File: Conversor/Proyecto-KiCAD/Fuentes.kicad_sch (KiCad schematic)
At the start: 17 parts, among them J6 Barrel_Jack_Switch, P1 SW_SPDT, P2 5V Header, P3 5V Header, P4 Jumper 2, U1 LP2985-3.3, U11 LM7805_TO252, U13 THB3-1211

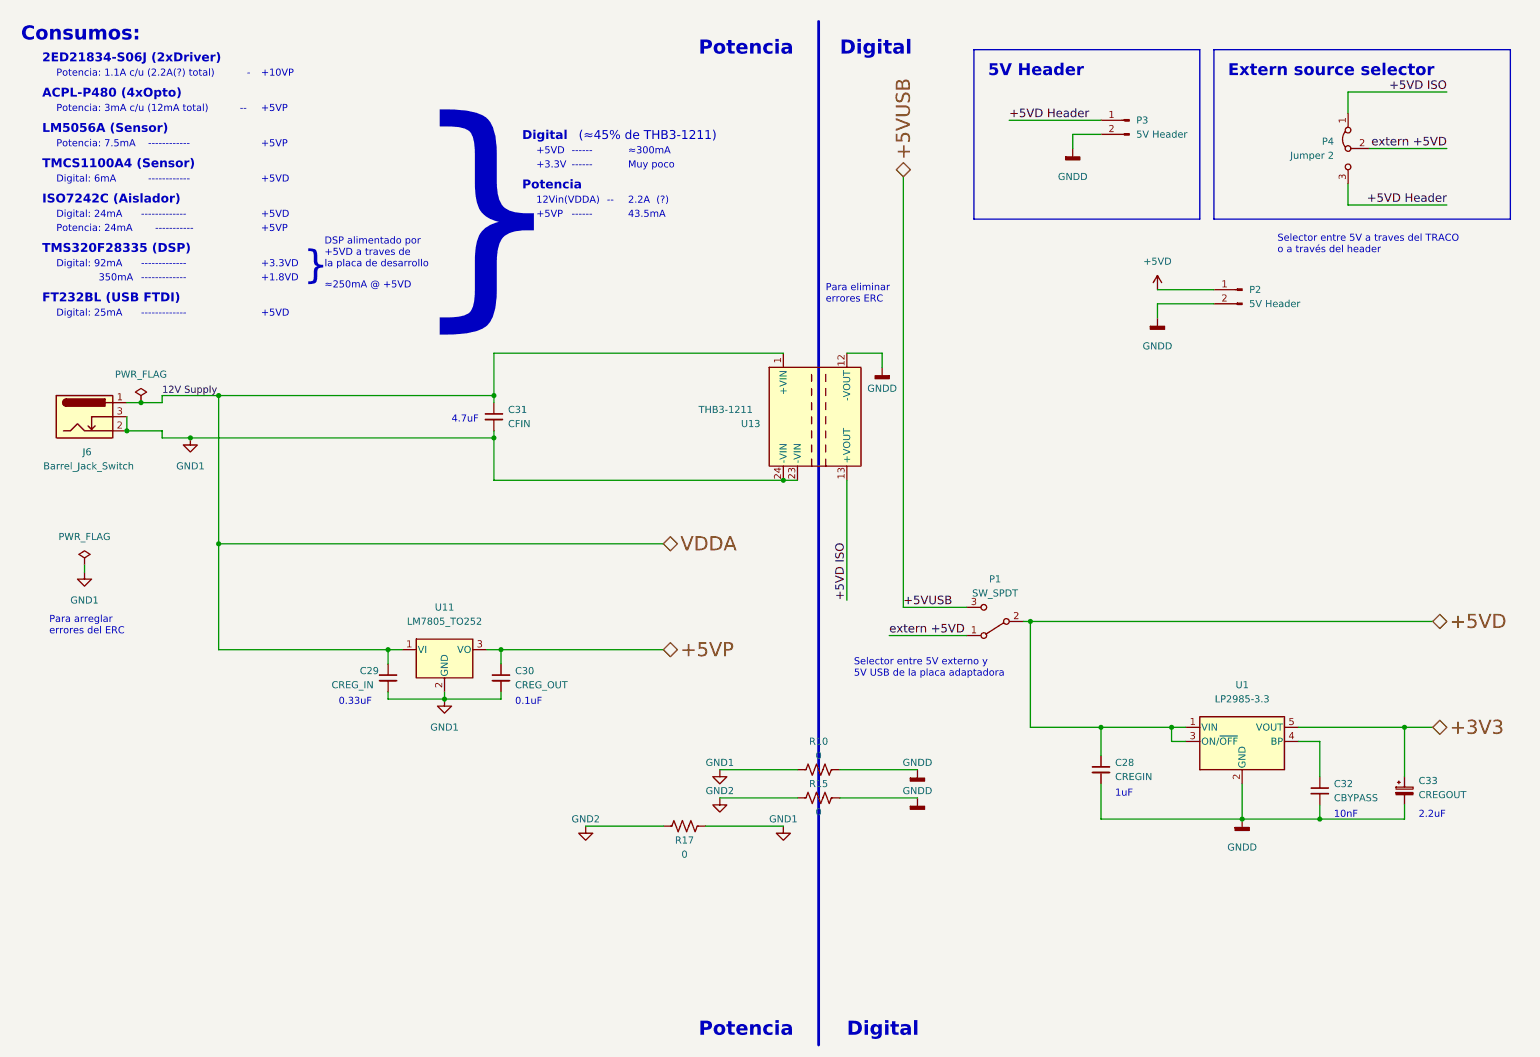
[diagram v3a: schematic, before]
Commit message: Agregar el selector de alim. de 12V y seguir emprolijando la placa
- Agregar modelos de los switches
- Agregar algunos test points
Por hacer:
  - Todo lo de los dos anteriores commits
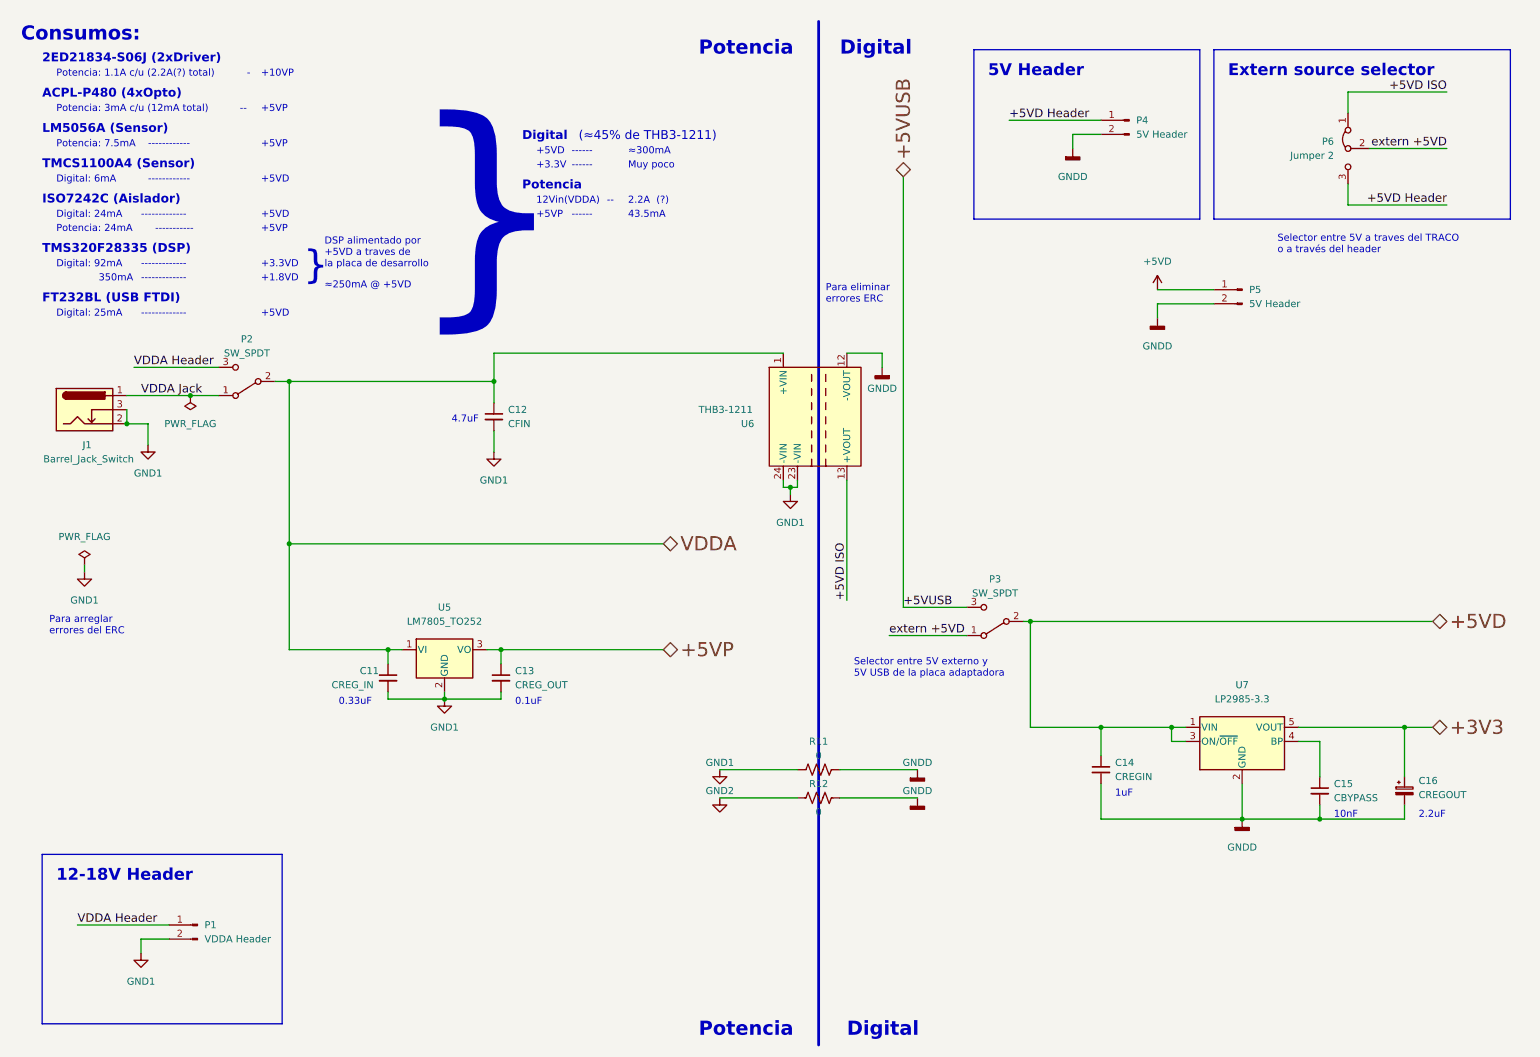
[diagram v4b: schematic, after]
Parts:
- removed R17: 0, Resistor_SMD:R_1206_3216Metric_Pad1.30x1.75mm_HandSolder, symbol Device:R_US
- added P1: VDDA Header, Connector_PinHeader_2.54mm:PinHeader_1x02_P2.54mm_Vertical, symbol Connector:Conn_01x02_Male
- added P2: SW_SPDT, Connector_PinHeader_2.54mm:PinHeader_1x03_P2.54mm_Vertical, symbol Switch:SW_SPDT
- renumbered C29 to C11, C31 to C12, C30 to C13, C28 to C14, C32 to C15, C33 to C16, J6 to J1, P1 to P3, P3 to P4, P2 to P5, P4 to P6, R10 to R11, R15 to R12, U11 to U5, U13 to U6, U1 to U7
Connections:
- net GND1: now also P1.2 (Pin_2)
- net VDDA: now also P2.2 (B); no longer J1.1
- new net VDDA Header: P1.1 (Pin_1), P2.3 (C)
- new net VDDA Jack: J1.1, P2.1 (A)
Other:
- note added: "12-18V Header"
- moved on the sheet: J1

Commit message: Agregar conectores de 12V y 5V, y seguir mas layout recommendations
- Ademas, seguir emprolijando la placa
- Agregar esquinas redondeadas a la placa
- Por hacer:
  - Ver las recomendaciones de Jorge
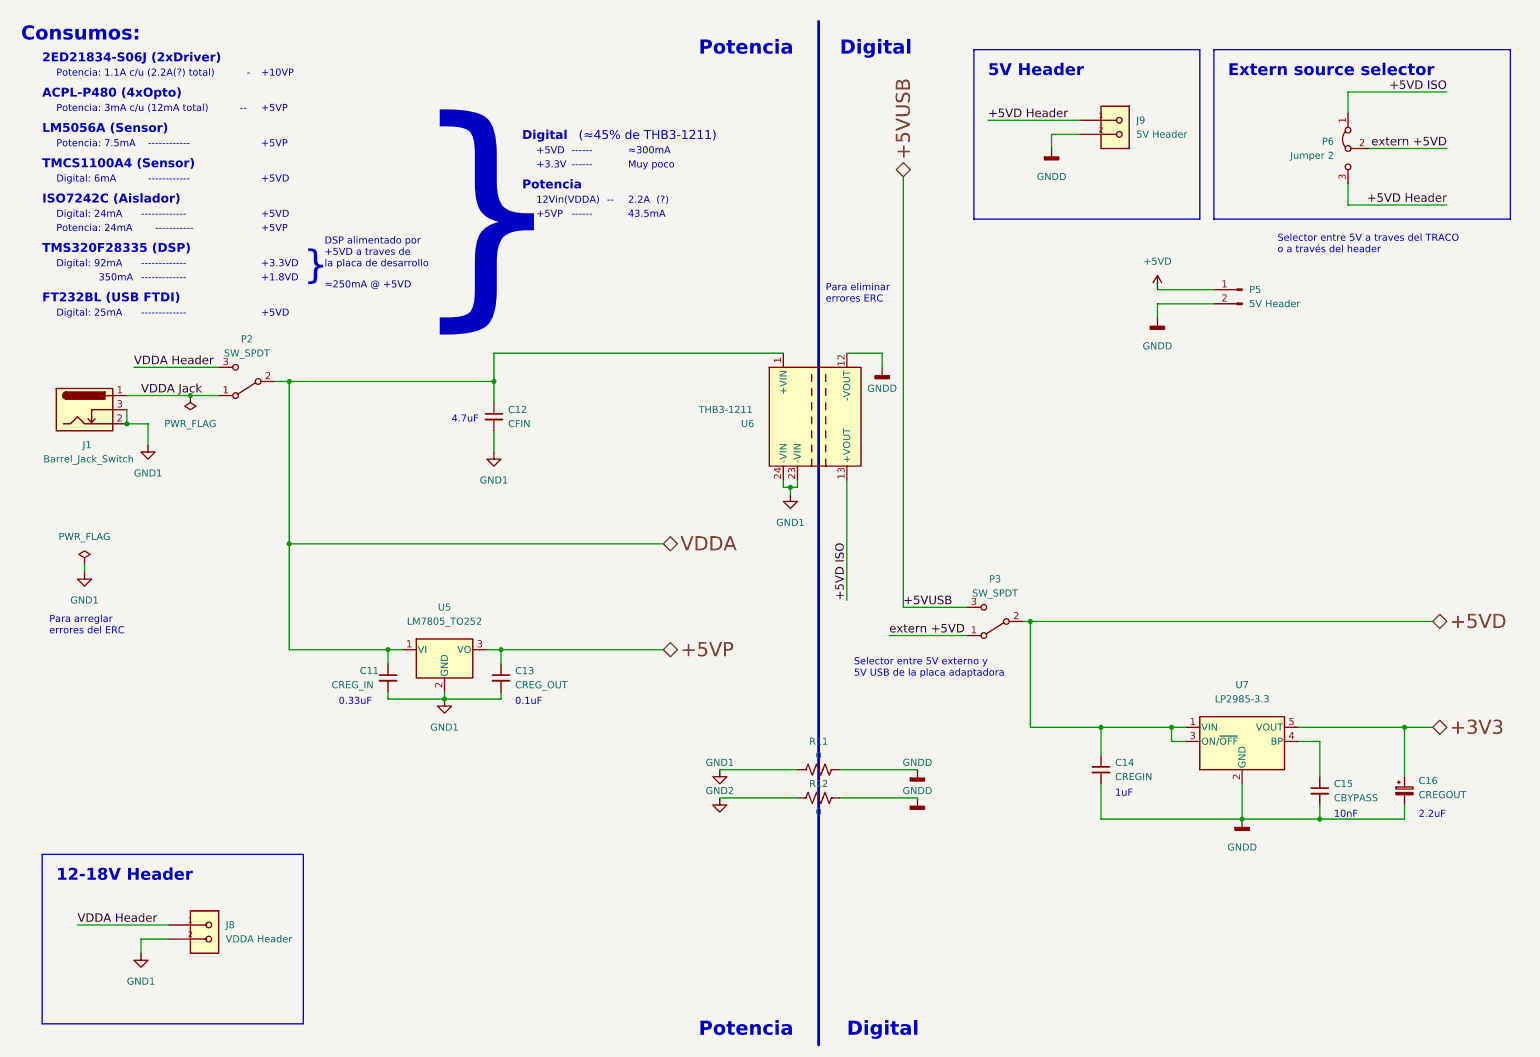
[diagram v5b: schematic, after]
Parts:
- removed P1: VDDA Header, Connector_PinHeader_2.54mm:PinHeader_1x02_P2.54mm_Vertical, symbol Connector:Conn_01x02_Male
- removed P4: 5V Header, Connector_PinHeader_2.54mm:PinHeader_1x02_P2.54mm_Vertical, symbol Connector:Conn_01x02_Male
- added J8: VDDA Header, 1725656, symbol 1725656:1725656
- added J9: 5V Header, 1725656, symbol 1725656:1725656
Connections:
- net +5VD Header: now also J9.1
- net GND1: now also J8.2
- net GNDD: now also J9.2
- net VDDA Header: now also J8.1
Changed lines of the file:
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@@
     (stroke (width 0) (type default) (color 0 0 0 0))
   )
-  (wire (pts (xy 190.5 30.48) (xy 207.01 30.48))
+  (wire (pts (xy 186.69 30.48) (xy 203.2 30.48))
     (stroke (width 0) (type default) (color 0 0 0 0))
   )
@@
     (stroke (width 0) (type default) (color 0 0 0 0))
   )
-  (polyline (pts (xy 59.69 193.04) (xy 59.69 162.56))
+  (polyline (pts (xy 63.5 193.04) (xy 63.5 162.56))
     (stroke (width 0) (type default) (color 0 0 0 0))
   )
@@
     (stroke (width 0) (type default) (color 0 0 0 0))
   )
-  (polyline (pts (xy 16.51 193.04) (xy 59.69 193.04))
+  (polyline (pts (xy 16.51 193.04) (xy 63.5 193.04))
     (stroke (width 0) (type default) (color 0 0 0 0))
   )
@@
     (stroke (width 0) (type default) (color 0 0 0 0))
   )
-  (wire (pts (xy 201.93 35.56) (xy 201.93 33.02))
+  (wire (pts (xy 198.12 35.56) (xy 198.12 33.02))
     (stroke (width 0) (type default) (color 0 0 0 0))
   )
@@
     (stroke (width 0) (type default) (color 0 0 0 0))
   )
-  (wire (pts (xy 201.93 33.02) (xy 207.01 33.02))
-    (stroke (width 0) (type default) (color 0 0 0 0))
-  )
-  (polyline (pts (xy 59.69 162.56) (xy 16.51 162.56))
+  (wire (pts (xy 198.12 33.02) (xy 203.2 33.02))
+    (stroke (width 0) (type default) (color 0 0 0 0))
+  )
+  (polyline (pts (xy 63.5 162.56) (xy 16.51 162.56))
     (stroke (width 0) (type default) (color 0 0 0 0))
   )
@@
     (effects (font (size 1.524 1.524)) (justify left bottom))
   )
-  (label "+5VD Header" (at 190.5 30.48 0)
+  (label "+5VD Header" (at 186.69 30.48 0)
     (effects (font (size 1.524 1.524)) (justify left bottom))
   )
@@
     (effects (font (size 2.54 2.54)) (justify left))
   )
-  (symbol (lib_id "power:GNDD") (at 201.93 35.56 0) (unit 1)
-    (in_bom yes) (on_board yes) (fields_autoplaced)
-    (property "Reference" "#PWR038" (id 0) (at 201.93 41.91 0)
-      (effects (font (size 1.27 1.27)) hide)
-    )
-    (property "Value" "GNDD" (id 1) (at 201.93 40.64 0))
-    (property "Footprint" "" (id 2) (at 201.93 35.56 0)
-      (effects (font (size 1.27 1.27)) hide)
-    )
-    (property "Datasheet" "" (id 3) (at 201.93 35.56 0)
+  (symbol (lib_id "power:GNDD") (at 198.12 35.56 0) (unit 1)
+    (in_bom yes) (on_board yes) (fields_autoplaced)
+    (property "Reference" "#PWR038" (id 0) (at 198.12 41.91 0)
+      (effects (font (size 1.27 1.27)) hide)
+    )
+    (property "Value" "GNDD" (id 1) (at 198.12 40.64 0))
+    (property "Footprint" "" (id 2) (at 198.12 35.56 0)
+      (effects (font (size 1.27 1.27)) hide)
+    )
+    (property "Datasheet" "" (id 3) (at 198.12 35.56 0)
       (effects (font (size 1.27 1.27)) hide)
     )
@@
     )
     (pin "1")
+  )
+  (symbol (lib_id "1725656:1725656") (at 208.28 30.48 180) (unit 1)
+    (in_bom yes) (on_board yes) (fields_autoplaced)
+    (property "Reference" "J9" (id 0) (at 213.36 30.4799 0)
+      (effects (font (size 1.27 1.27)) (justify right))
+    )
+    (property "Value" "5V Header" (id 1) (at 213.36 33.0199 0)
+      (effects (font (size 1.27 1.27)) (justify right))
+    )
+    (property "Footprint" "1725656" (id 2) (at 208.28 30.48 0)
+      (effects (font (size 1.27 1.27)) (justify left bottom) hide)
+    )
+    (property "Datasheet" "" (id 3) (at 208.28 30.48 0)
+      (effects (font (size 1.27 1.27)) (justify left bottom) hide)
+    )
+    (pin "1")
+    (pin "2")
   )
   (symbol (lib_id "Device:C_Small") (at 97.79 83.82 0) (unit 1)
@@
     (pin "3")
   )
-  (symbol (lib_id "Connector:Conn_01x02_Male") (at 44.45 175.26 0) (mirror y) (unit 1)
-    (in_bom yes) (on_board yes) (fields_autoplaced)
-    (property "Reference" "P1" (id 0) (at 45.72 175.2599 0)
+  (symbol (lib_id "1725656:1725656") (at 44.45 175.26 180) (unit 1)
+    (in_bom yes) (on_board yes) (fields_autoplaced)
+    (property "Reference" "J8" (id 0) (at 49.53 175.2599 0)
       (effects (font (size 1.27 1.27)) (justify right))
     )
-    (property "Value" "VDDA Header" (id 1) (at 45.72 177.7999 0)
+    (property "Value" "VDDA Header" (id 1) (at 49.53 177.7999 0)
       (effects (font (size 1.27 1.27)) (justify right))
     )
-    (property "Footprint" "Connector_PinHeader_2.54mm:PinHeader_1x02_P2.54mm_Vertical" (id 2) (at 44.45 175.26 0)
-      (effects (font (size 1.27 1.27)) hide)
-    )
-    (property "Datasheet" "~" (id 3) (at 44.45 175.26 0)
-      (effects (font (size 1.27 1.27)) hide)
+    (property "Footprint" "1725656" (id 2) (at 44.45 175.26 0)
+      (effects (font (size 1.27 1.27)) (justify left bottom) hide)
+    )
+    (property "Datasheet" "" (id 3) (at 44.45 175.26 0)
+      (effects (font (size 1.27 1.27)) (justify left bottom) hide)
     )
     (pin "1")
@@
       (effects (font (size 1.27 1.27)) hide)
     )
-    (pin "1")
-    (pin "2")
-  )
-  (symbol (lib_id "Connector:Conn_01x02_Male") (at 212.09 30.48 0) (mirror y) (unit 1)
-    (in_bom yes) (on_board yes) (fields_autoplaced)
-    (property "Reference" "P4" (id 0) (at 213.36 30.4799 0)
-      (effects (font (size 1.27 1.27)) (justify right))
-    )
-    (property "Value" "5V Header" (id 1) (at 213.36 33.0199 0)
-      (effects (font (size 1.27 1.27)) (justify right))
-    )
-    (property "Footprint" "Connector_PinHeader_2.54mm:PinHeader_1x02_P2.54mm_Vertical" (id 2) (at 212.09 30.48 0)
-      (effects (font (size 1.27 1.27)) hide)
-    )
-    (property "Datasheet" "~" (id 3) (at 212.09 30.48 0)
-      (effects (font (size 1.27 1.27)) hide)
-    )
